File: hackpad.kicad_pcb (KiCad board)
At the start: 2 copper layers, 68 x 99.7 mm, 25 parts, among them J1 Conn_01x04, SW1 SW_Push, SW10 RotaryEncoder_Switch, SW2 SW_Push, SW3 SW_Push, SW4 SW_Push, SW5 SW_Push, SW6 SW_Push, SW7 SW_Push, SW8 SW_Push, SW9 SW_Push, U1 MOUDLE-SEEEDUINO-XIAO

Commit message: Add MIT license, finalize DRC-clean PCB, export JLCPCB gerbers
- LICENSE: MIT covering software + hardware
- README: license section -> MIT
- PCB now DRC-clean (GND pour refilled, ENC_SW reconnected, stray
  GND track over encoder MP pad removed); only intentional baseline
  notices remain
- export/hackpad-gerbers.zip: fab-ready gerbers + Excellon drill

Co-Authored-By: Claude Opus 4.8 <noreply@anthropic.com>
Claude-Session: https://claude.ai/code/session_01VPvtJRWkd5XUxsE6SwSzo5
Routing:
- net /ENC_B: track 113.5 -> 105.4 mm
- net /ENC_SW: track 103.5 -> 100.5 mm
- net /GND: track 225.8 -> 227.6 mm
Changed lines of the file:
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@@
-	)
-	(segment
-		(start 73.74 23.903654)
-		(end 70.576346 20.74)
-		(width 0.2)
-		(layer "F.Cu")
-		(net "/GND")
-	)
-	(segment
-		(start 60.54 107.52)
-		(end 60.54 106.5)
-		(width 0.2)
-		(layer "F.Cu")
-		(net "/GND")
 	)
 	(segment
@@
 	)
 	(segment
-		(start 72.64 93.485686)
-		(end 72.64 22.803654)
+		(start 64.35 105.82)
+		(end 72.64 97.53)
+		(width 0.2)
+		(layer "F.Cu")
+		(net "/GND")
+	)
+	(segment
+		(start 72.64 22.803654)
+		(end 70.576346 20.74)
+		(width 0.2)
+		(layer "F.Cu")
+		(net "/GND")
+	)
+	(segment
+		(start 59.25 105.82)
+		(end 64.35 105.82)
 		(width 0.2)
 		(layer "F.Cu")
@@
 	)
 	(segment
-		(start 59.86 105.82)
-		(end 60.54 106.5)
-		(width 0.2)
-		(layer "F.Cu")
-		(net "/GND")
-	)
-	(segment
-		(start 60.54 105.585686)
-		(end 72.64 93.485686)
-		(width 0.2)
-		(layer "F.Cu")
-		(net "/GND")
-	)
-	(segment
-		(start 73.74 106.32)
-		(end 73.74 23.903654)
-		(width 0.2)
-		(layer "F.Cu")
-		(net "/GND")
-	)
-	(segment
-		(start 60.54 106.5)
-		(end 60.54 105.585686)
-		(width 0.2)
-		(layer "F.Cu")
-		(net "/GND")
-	)
-	(segment
-		(start 72.64 22.803654)
-		(end 70.576346 20.74)
-		(width 0.2)
-		(layer "F.Cu")
+		(start 72.64 97.53)
+		(end 72.64 22.803654)
+		(width 0.2)
+		(layer "F.Cu")
+		(net "/GND")
+	)
+	(segment
+		(start 73.75 103.32)
+		(end 77.29 99.78)
+		(width 0.2)
+		(layer "B.Cu")
 		(net "/GND")
 	)
@@
 	)
 	(segment
+		(start 77.29 27.453654)
+		(end 70.576346 20.74)
+		(width 0.2)
+		(layer "B.Cu")
+		(net "/GND")
+	)
+	(segment
+		(start 70.576346 20.74)
+		(end 69.49 20.74)
+		(width 0.2)
+		(layer "B.Cu")
+		(net "/GND")
+	)
+	(segment
 		(start 31.13 14.87)
 		(end 63.62 14.87)
@@
 	)
 	(segment
+		(start 77.29 99.78)
+		(end 77.29 27.453654)
+		(width 0.2)
+		(layer "B.Cu")
+		(net "/GND")
+	)
+	(segment
 		(start 31.72 16.82)
 		(end 33.27 15.27)
@@
 	)
 	(segment
+		(start 57.95 81.55)
+		(end 59.095051 80.404949)
+		(width 0.2)
+		(layer "F.Cu")
+		(net "/ENC_B")
+	)
+	(segment
 		(start 68.169899 86.32)
 		(end 69.9 84.589899)
@@
 	)
 	(segment
-		(start 59.24 108.32)
-		(end 57.94 109.62)
+		(start 57.95 107.02)
+		(end 57.95 81.55)
 		(width 0.2)
 		(layer "F.Cu")
@@
 	)
 	(segment
-		(start 57.94 77.249899)
+		(start 61.095051 80.404949)
 		(end 67.010101 86.32)
-		(width 0.2)
-		(layer "F.Cu")
-		(net "/ENC_B")
-	)
-	(segment
-		(start 57.94 110.02)
-		(end 57.94 109.62)
 		(width 0.2)
 		(layer "F.Cu")
@@
 	)
 	(segment
-		(start 57.94 109.62)
-		(end 57.94 77.249899)
-		(width 0.2)
-		(layer "F.Cu")
-		(net "/ENC_B")
-	)
-	(segment
 		(start 64.687843 33.162157)
 		(end 69.49 28.36)
@@
 	)
 	(segment
+		(start 59.095051 80.404949)
+		(end 61.095051 80.404949)
+		(width 0.2)
+		(layer "F.Cu")
+		(net "/ENC_B")
+	)
+	(segment
 		(start 68.99 47.399899)
 		(end 68.99 37.464314)
@@
 	)
 	(segment
+		(start 59.25 108.32)
+		(end 57.95 107.02)
+		(width 0.2)
+		(layer "F.Cu")
+		(net "/ENC_B")
+	)
+	(segment
 		(start 69.9 84.589899)
 		(end 69.9 74.535256)
@@
 	)
 	(segment
+		(start 73.75 108.32)
+		(end 75.05 107.02)
+		(width 0.2)
+		(layer "F.Cu")
+		(net "/ENC_SW")
+	)
+	(segment
+		(start 68.34 24.67)
+		(end 69.49 25.82)
+		(width 0.2)
+		(layer "F.Cu")
+		(net "/ENC_SW")
+	)
+	(segment
+		(start 69.013654 19.59)
+		(end 68.34 20.263654)
+		(width 0.2)
+		(layer "F.Cu")
+		(net "/ENC_SW")
+	)
+	(segment
+		(start 75.05 107.02)
+		(end 75.05 22.673654)
+		(width 0.2)
+		(layer "F.Cu")
+		(net "/ENC_SW")
+	)
+	(segment
 		(start 71.966346 19.59)
 		(end 69.013654 19.59)
@@
 	)
 	(segment
-		(start 68.34 24.67)
-		(end 69.49 25.82)
+		(start 75.05 22.673654)
+		(end 71.966346 19.59)
 		(width 0.2)
 		(layer "F.Cu")
@@
 		(start 68.34 20.263654)
 		(end 68.34 24.67)
-		(width 0.2)
-		(layer "F.Cu")
-		(net "/ENC_SW")
-	)
-	(segment
-		(start 73.74 108.32)
-		(end 75.04 109.62)
-		(width 0.2)
-		(layer "F.Cu")
-		(net "/ENC_SW")
-	)
-	(segment
-		(start 75.04 110.02)
-		(end 75.04 109.62)
-		(width 0.2)
-		(layer "F.Cu")
-		(net "/ENC_SW")
-	)
-	(segment
-		(start 75.04 22.663654)
-		(end 71.966346 19.59)
-		(width 0.2)
-		(layer "F.Cu")
-		(net "/ENC_SW")
-	)
-	(segment
-		(start 69.013654 19.59)
-		(end 68.34 20.263654)
-		(width 0.2)
-		(layer "F.Cu")
-		(net "/ENC_SW")
-	)
-	(segment
-		(start 75.04 109.62)
-		(end 75.04 22.663654)
 		(width 0.2)
 		(layer "F.Cu")
@@
 		(polygon
 			(pts
-				(xy 36 113) (xy 79.02495 112.633974) (xy 83 112) (xy 82.193881 12.938263) (xy 14 13.5) (xy 13.59916 74.370272)
-				(xy 14.375777 113.429951)
+				(xy 12.641822 114.240731) (xy 43.063624 114.642849) (xy 84 114.5) (xy 83.423074 13.104991) (xy 12 12)
+				(xy 12 74.370272)
 			)
 		)

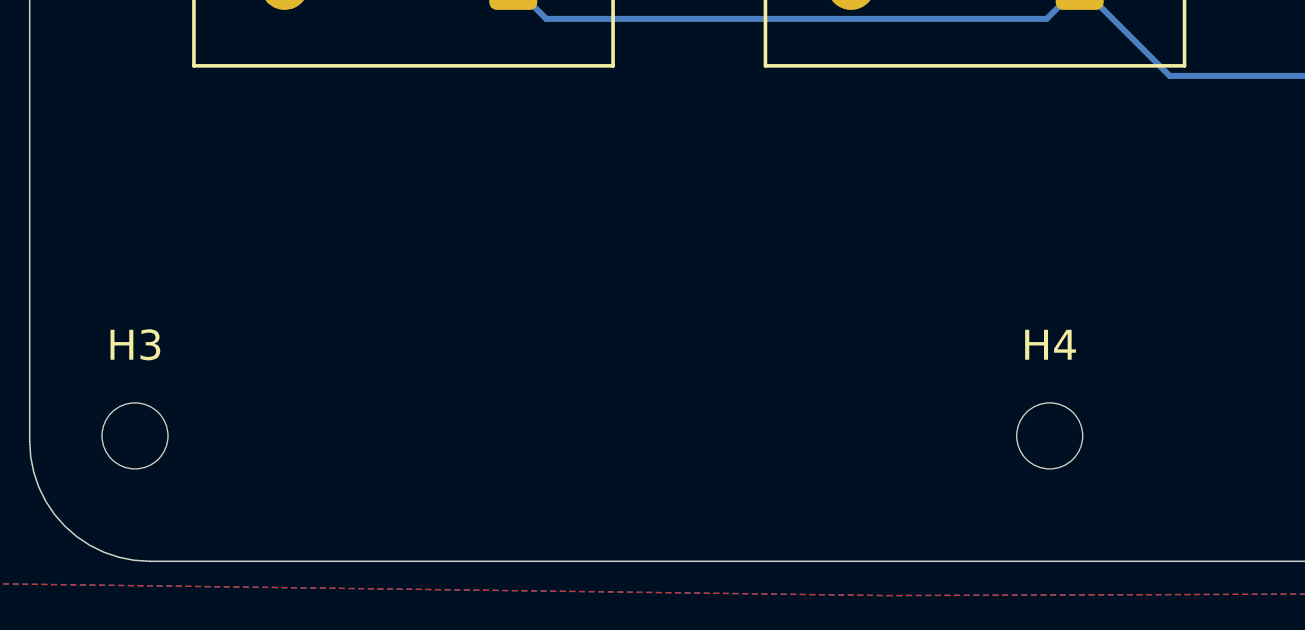
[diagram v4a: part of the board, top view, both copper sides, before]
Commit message: Add "LG Hackpad" branding to PCB silkscreen, re-export gerbers
Front silkscreen now carries the macropad name (required for YSWS
submission). PCB still DRC-clean. Regenerated export/hackpad-gerbers.zip.

Co-Authored-By: Claude Opus 4.8 <noreply@anthropic.com>
Claude-Session: https://claude.ai/code/session_01VPvtJRWkd5XUxsE6SwSzo5
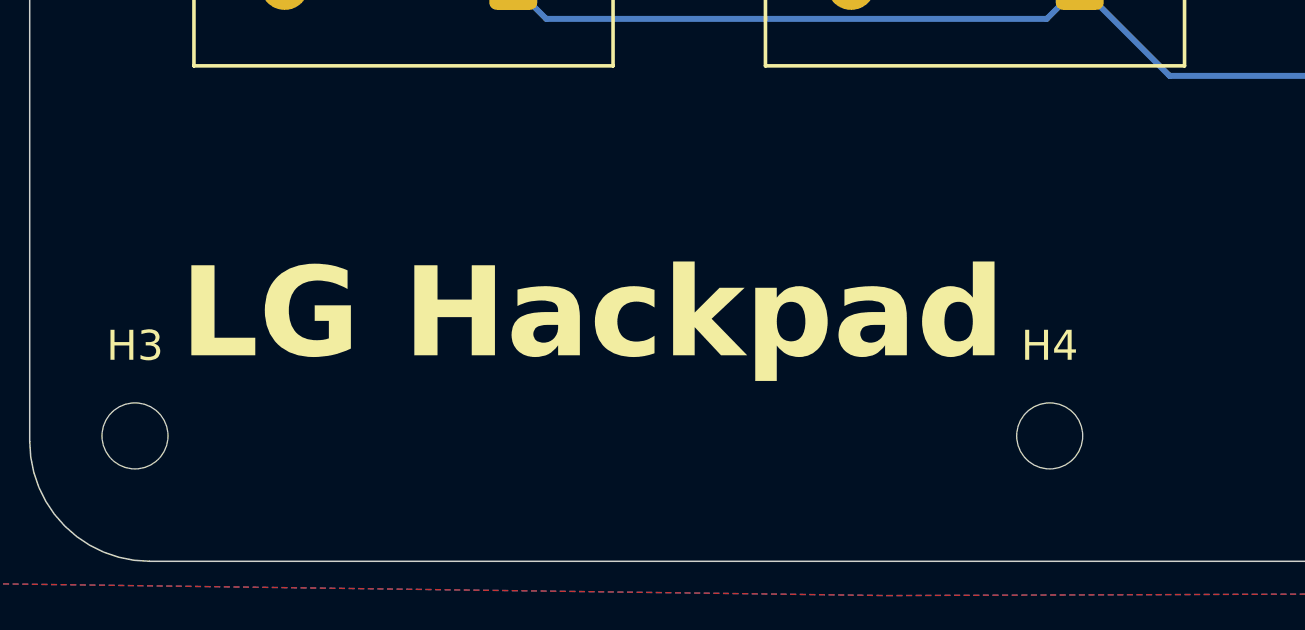
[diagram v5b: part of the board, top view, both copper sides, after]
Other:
- board text added: "LG Hackpad"
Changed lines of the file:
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@@
 		(layer "Edge.Cuts")
+	)
+	(gr_text "LG Hackpad"
+		(at 19.5 107 0)
+		(layer "F.SilkS")
+		(effects
+			(font
+				(size 3 3)
+				(thickness 0.3)
+				(bold yes)
+			)
+			(justify left bottom)
+		)
 	)
 	(segment
